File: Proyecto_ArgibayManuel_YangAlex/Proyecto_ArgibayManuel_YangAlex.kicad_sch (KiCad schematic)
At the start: 45 parts, among them IC1 LM1117, J1 Conn_01x09, J2 Conn_01x08, K1 RT314012, K2 RT314012, Q1 2N2222, Q2 2N2222, SW1 SW_Push, SW2 SW_Push, SW3 SW_Push, SW4 SW_Push, SW5 SW_Push, SW6 SW_Push, U1 PIC18F258-I_SO, U10 LT1716IS5TRMPBF, U2 DRV8871DDA, U3 DRV8871DDA, U6 MCP2551-I-P, U9 LT1716IS5TRMPBF, X1 DB9, Y1 Crystal

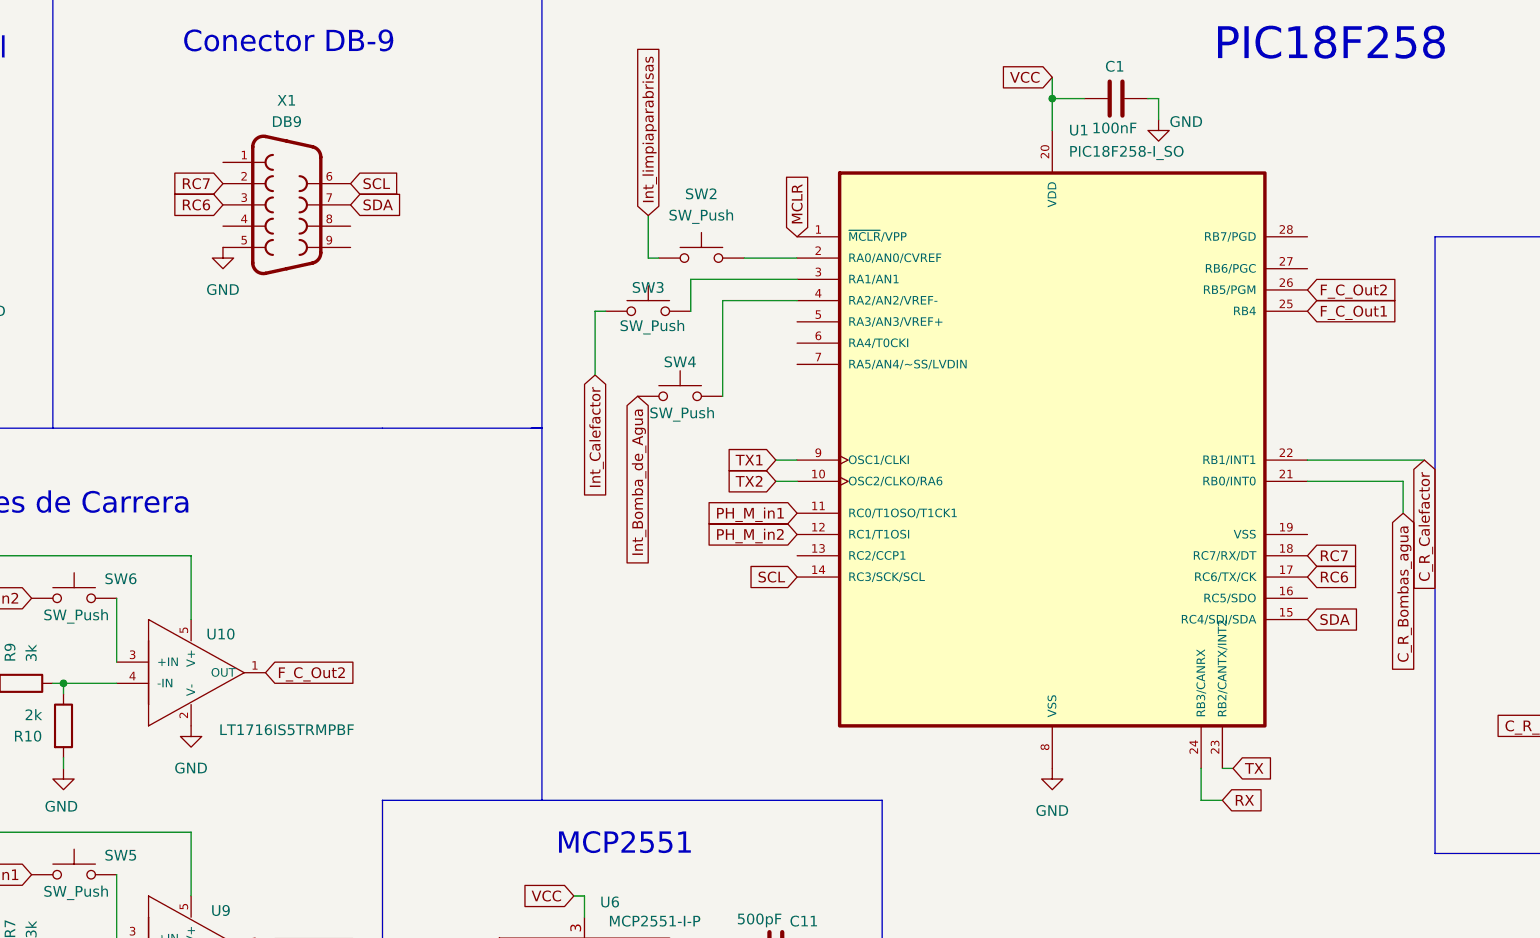
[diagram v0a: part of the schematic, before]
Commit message: Agrego net classes, proyecto y cambio de presentación
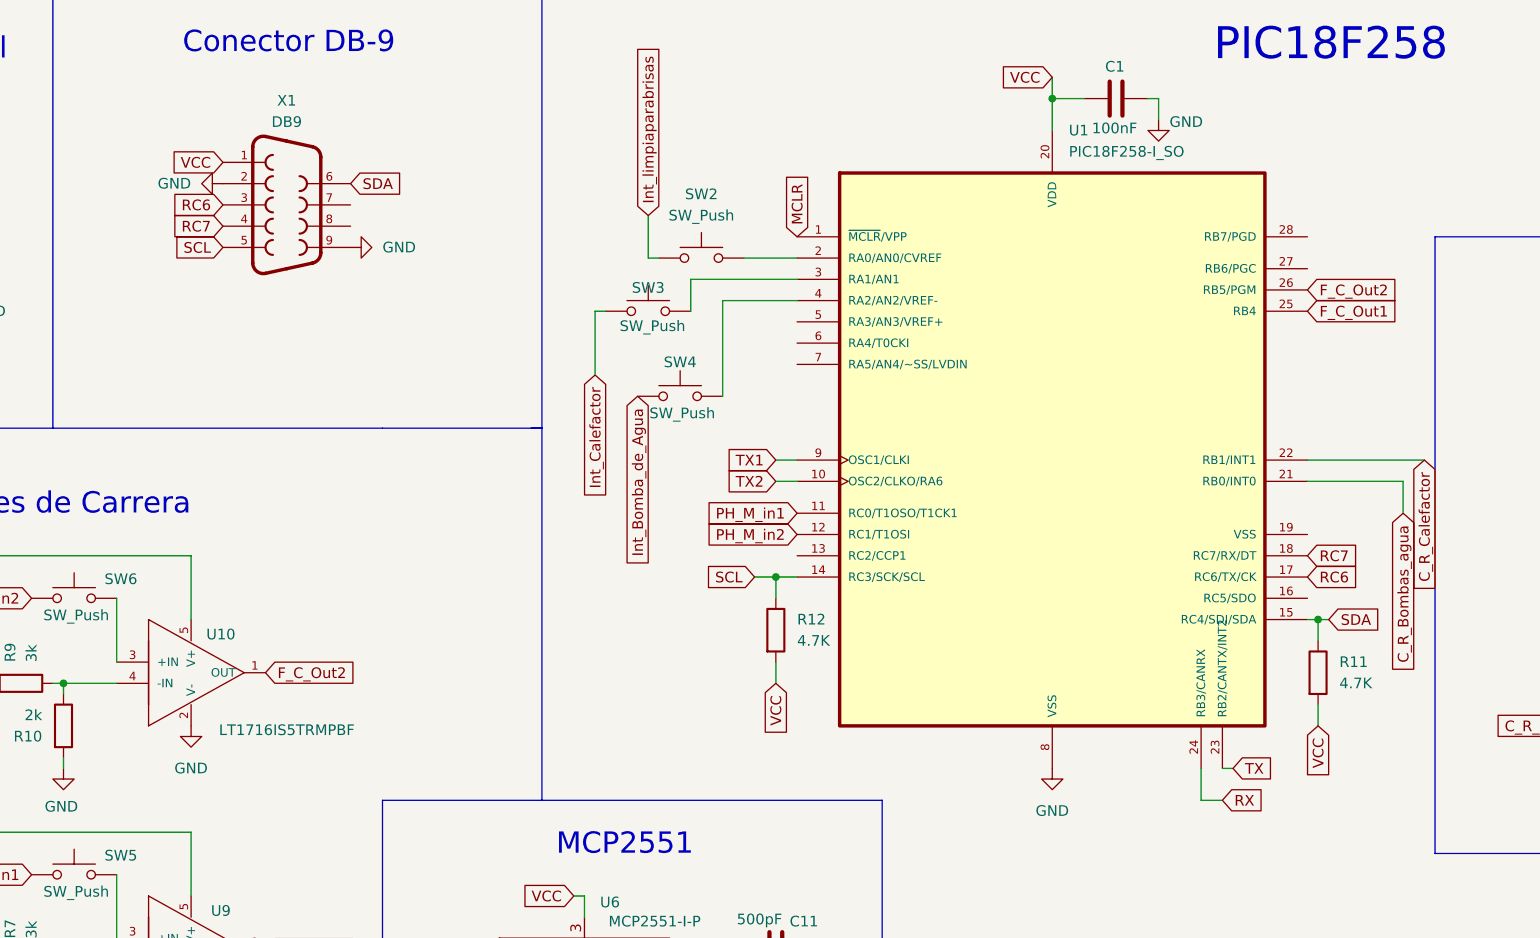
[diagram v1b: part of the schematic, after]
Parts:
- added R11, R12: 4.7K, symbol Device:R
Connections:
- net GND: now also X1.2, X1.9; no longer X1.5
- net RC7: now also X1.4; no longer X1.2
- net SCL: now also X1.5, R12.1; no longer X1.6
- net SDA: now also X1.6, R11.1; no longer X1.7
- net VCC: now also X1.1, R11.2, R12.2

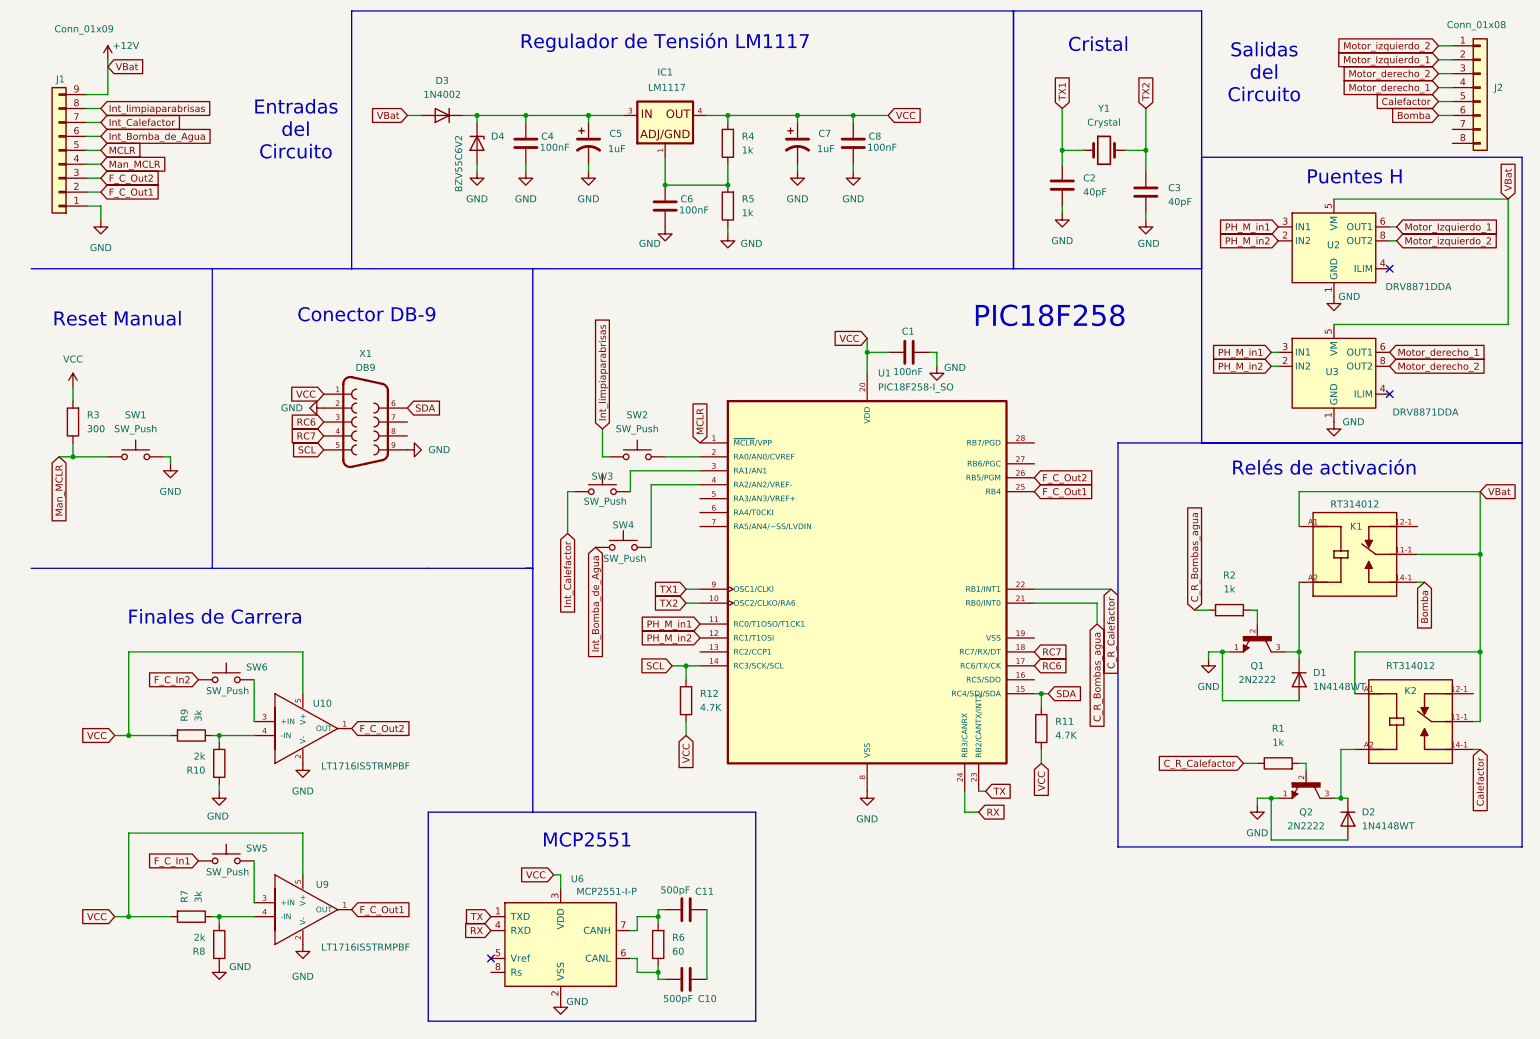
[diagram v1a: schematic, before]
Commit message: Modifique,netlist,Final de Carrera,GNDPWR,,seperar botonera
Cambios
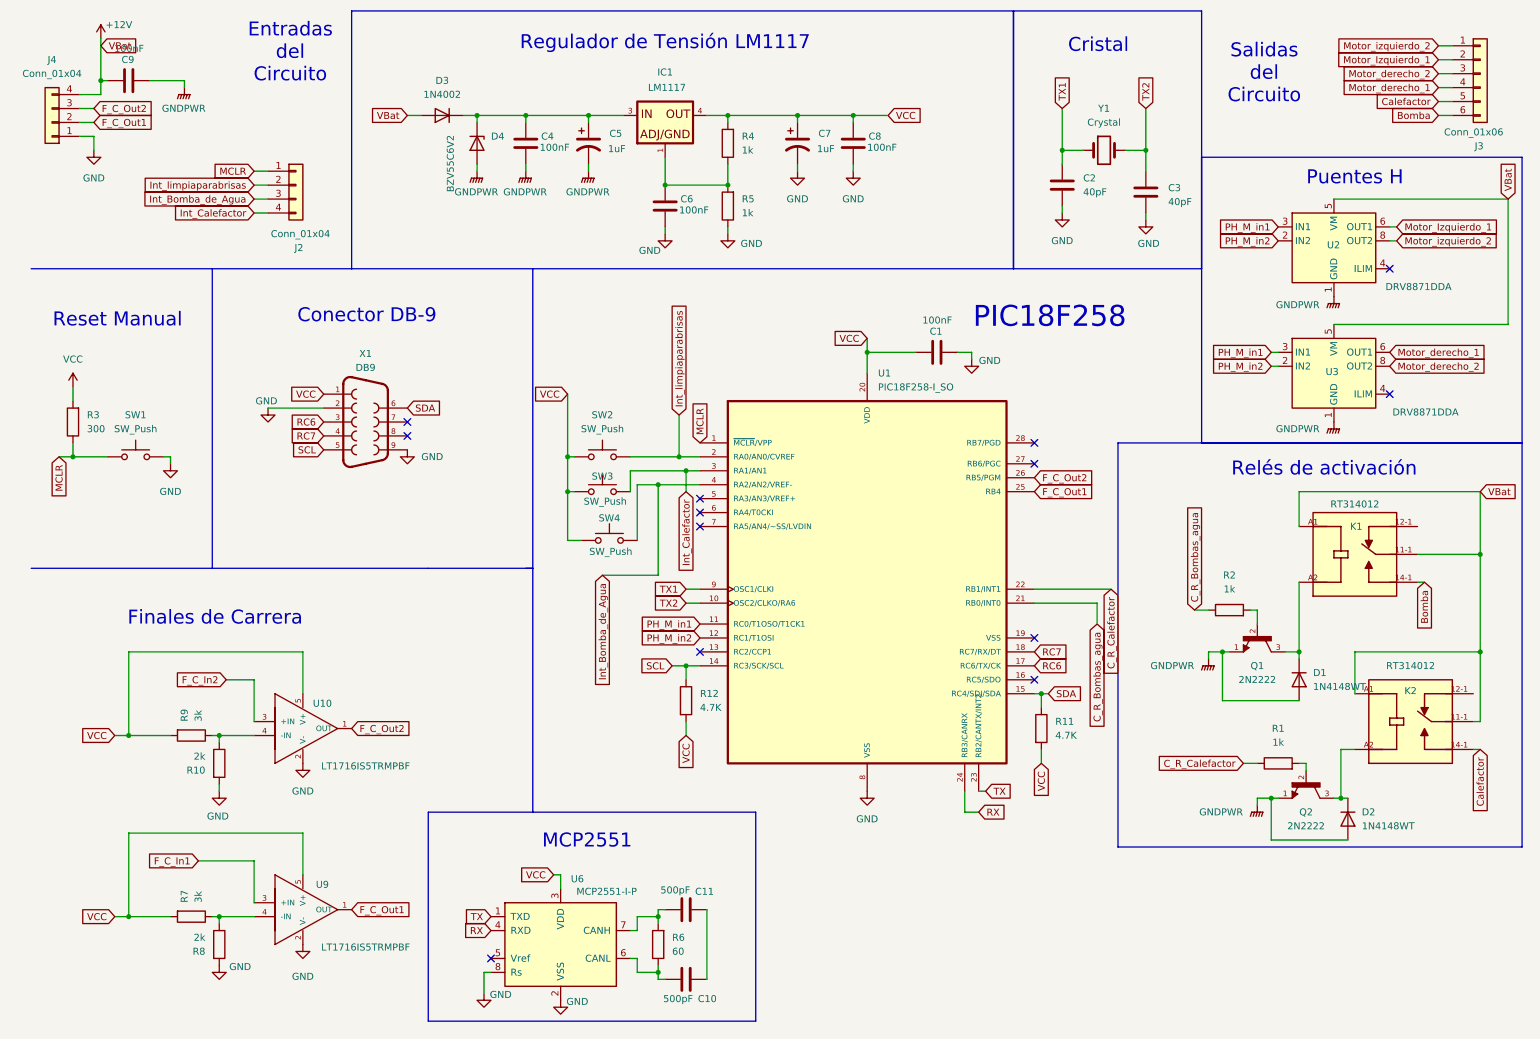
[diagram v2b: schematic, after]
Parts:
- removed J1: Conn_01x09, symbol Connector_Generic:Conn_01x09
- removed J2: Conn_01x08, symbol Connector_Generic:Conn_01x08
- removed SW5, SW6: SW_Push, symbol Switch:SW_Push
- added C9: 100nF, symbol Device:C
- added J2, J4: Conn_01x04, symbol Connector_Generic:Conn_01x04
- added J3: Conn_01x06, symbol Connector_Generic:Conn_01x06
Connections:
- net Man_MCLR is gone; now on net MCLR: R3.1, SW1.1
- net +12V: now also C9.1, J4.4 (Pin_4)
- net Bomba: now also J3.6 (Pin_6)
- net Calefactor: now also J3.5 (Pin_5)
- net F_C_In1: now also U9.3 (+IN)
- net F_C_In2: now also U10.3 (+IN)
- net F_C_Out1: now also J4.2 (Pin_2)
- net F_C_Out2: now also J4.3 (Pin_3)
- net GND: now also U6.8 (Rs), J4.1 (Pin_1); no longer C4.2, C5.2, D1.2 (A), D2.2 (A), D4.2 (A), Q1.1, Q2.1, U2.1 (GND), U2.7 (GND), U2.9 (GND), U3.1 (GND), U3.7 (GND), U3.9 (GND)
- net Int_Bomba_de_Agua: now also SW4.2, U1.4 (RA2/AN2/VREF-), J2.3 (Pin_3); no longer SW4.1
- net Int_Calefactor: now also SW3.2, U1.3 (RA1/AN1), J2.4 (Pin_4); no longer SW3.1
- net Int_limpiaparabrisas: now also SW2.2, U1.2 (RA0/AN0/CVREF), J2.2 (Pin_2); no longer SW2.1
- net MCLR: now also J2.1 (Pin_1)
- net Motor_Izquierdo_1: now also J3.2 (Pin_2)
- net Motor_derecho_1: now also J3.4 (Pin_4)
- net Motor_derecho_2: now also J3.3 (Pin_3)
- net Motor_izquierdo_2: now also J3.1 (Pin_1)
- net VCC: now also SW2.1, SW3.1, SW4.1
- new net GNDPWR: C4.2, C5.2, C9.2, D1.2 (A), D2.2 (A), D4.2 (A), Q1.1, Q2.1, U2.1 (GND), U2.7 (GND), U2.9 (GND), U3.1 (GND), U3.7 (GND), U3.9 (GND)
- no-connect marks 3 -> 13
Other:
- moved on the sheet: C1, SW2, SW4

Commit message: Separacion del circuito
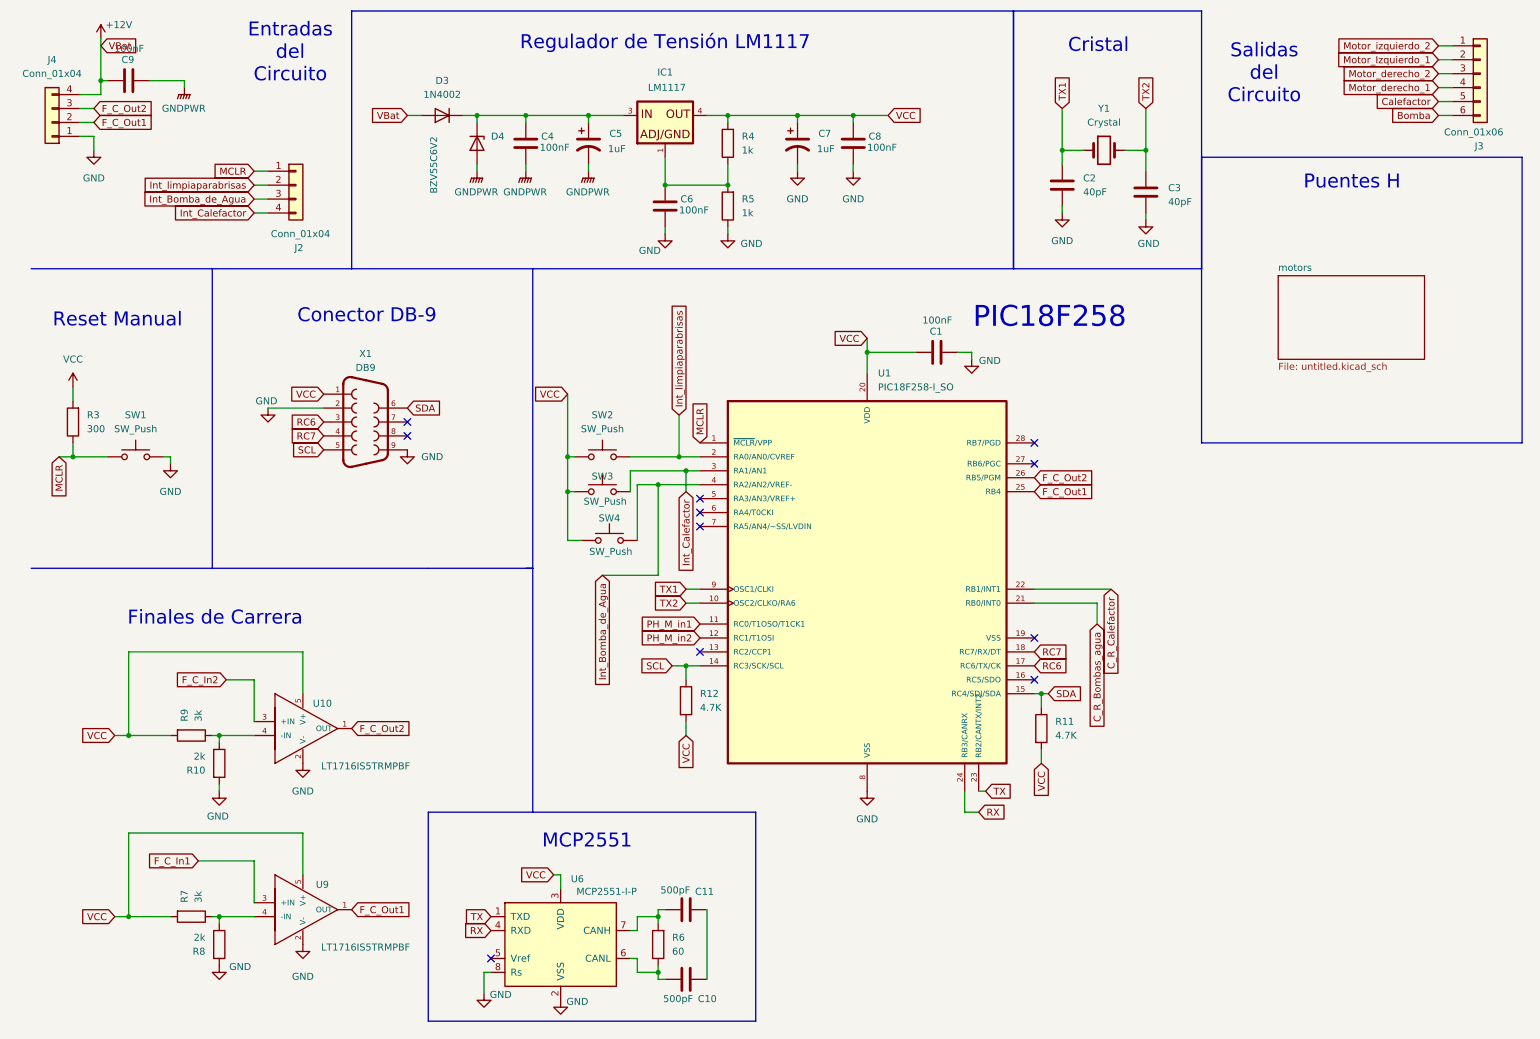
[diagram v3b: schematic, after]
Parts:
- removed D1, D2: 1N4148WT, Diode_SMD:D_SOD-523, symbol Diode:1N4148WT
- removed K1, K2: RT314012, RT314012:RELAY_9-1393239-5, symbol RT314012:RT314012
- removed Q1, Q2: 2N2222, 2N2222:TO127P580H530-3, symbol 2N2222:2N2222
- removed R1, R2: 1k, symbol Device:R
- removed U2, U3: DRV8871DDA, Package_SO:Texas_HTSOP-8-1EP_3.9x4.9mm_P1.27mm_EP2.95x4.9mm_Mask2.4x3.1mm_ThermalVias, symbol Driver_Motor:DRV8871DDA
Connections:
- no-connect marks 13 -> 11
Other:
- added sheet motors (untitled.kicad_sch)
- note removed: "Relés de activación"

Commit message: Modifico simulaciones del comparador y arreglo esquemático
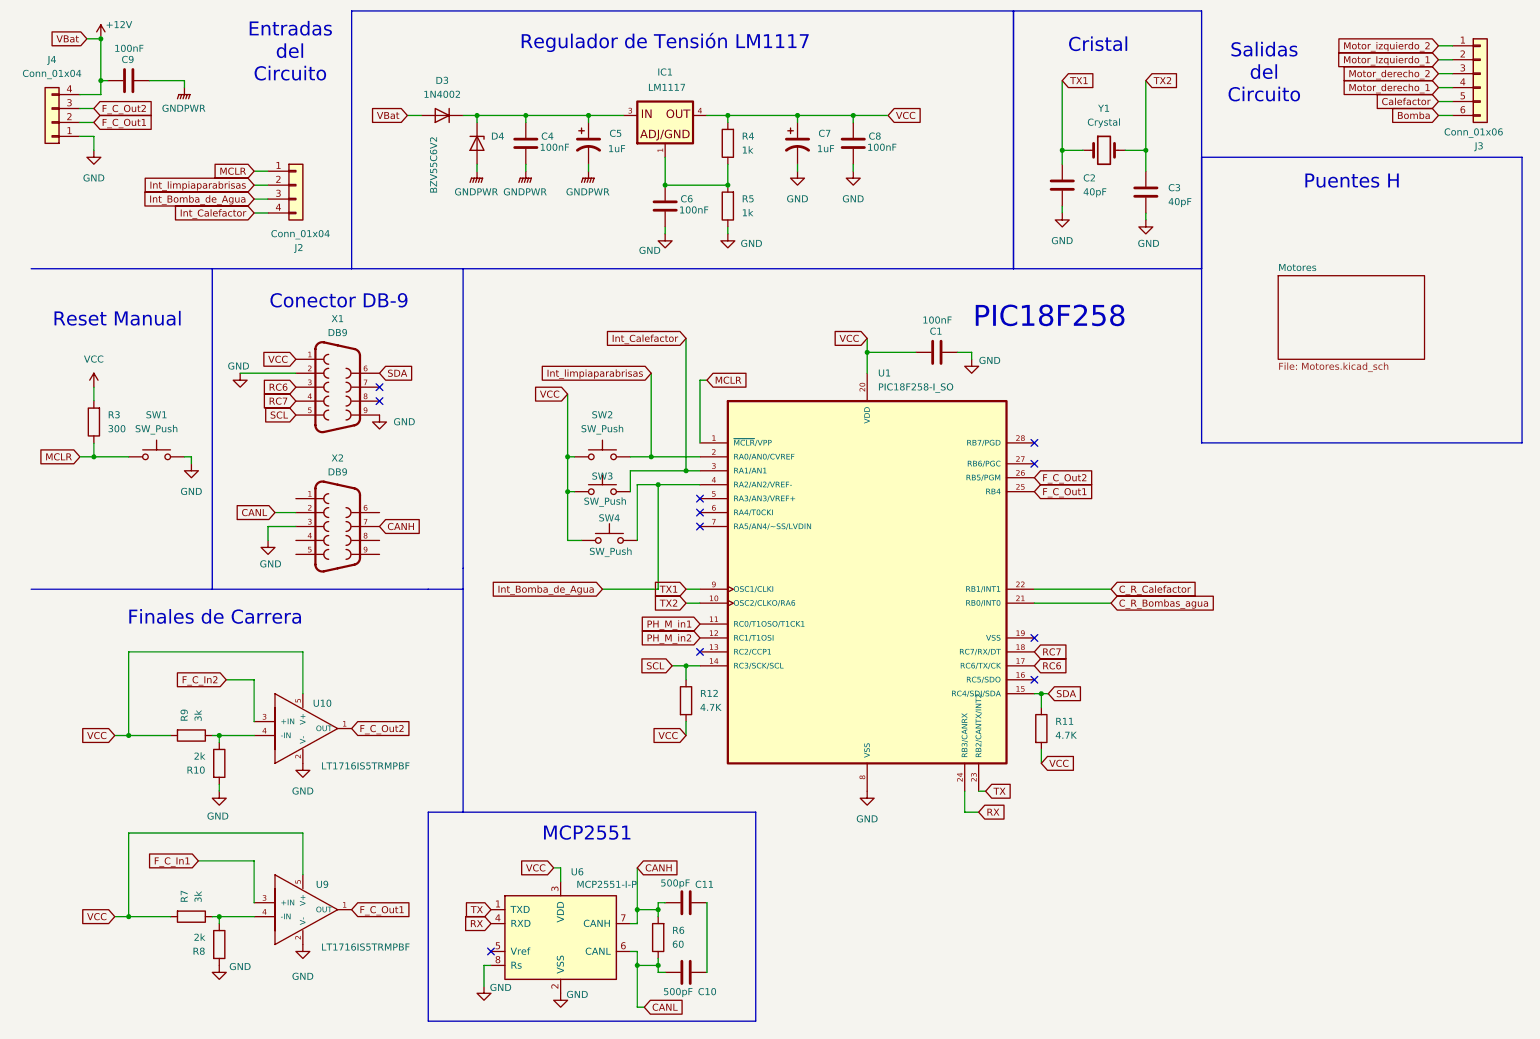
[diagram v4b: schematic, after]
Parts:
- added X2: DB9, DB9:DB9, symbol DB9:DB9
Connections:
- net GND: now also X2.3
- net CANL: now reaches C10.1, R6.1, U6.6 (CANL)
- net CANL: now also X2.2
- net CANH: now reaches C11.1, R6.2, U6.7 (CANH)
- net CANH: now also X2.7
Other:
- sheet motors renamed Motores
- sheet Motores: file untitled.kicad_sch -> Motores.kicad_sch
- moved on the sheet: C10, C11, R3, R6, SW1, U6, X1
